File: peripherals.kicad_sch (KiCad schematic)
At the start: 15 parts, among them J10 Cam 3, J11 Servo, J12 Cam 2, J2 Encoder, J9 Cam 1, Q1 BSS816NWH6327XTSA1, Q2 NPN, Q3 BSS816NWH6327XTSA1, Q6 BSS816NWH6327XTSA1

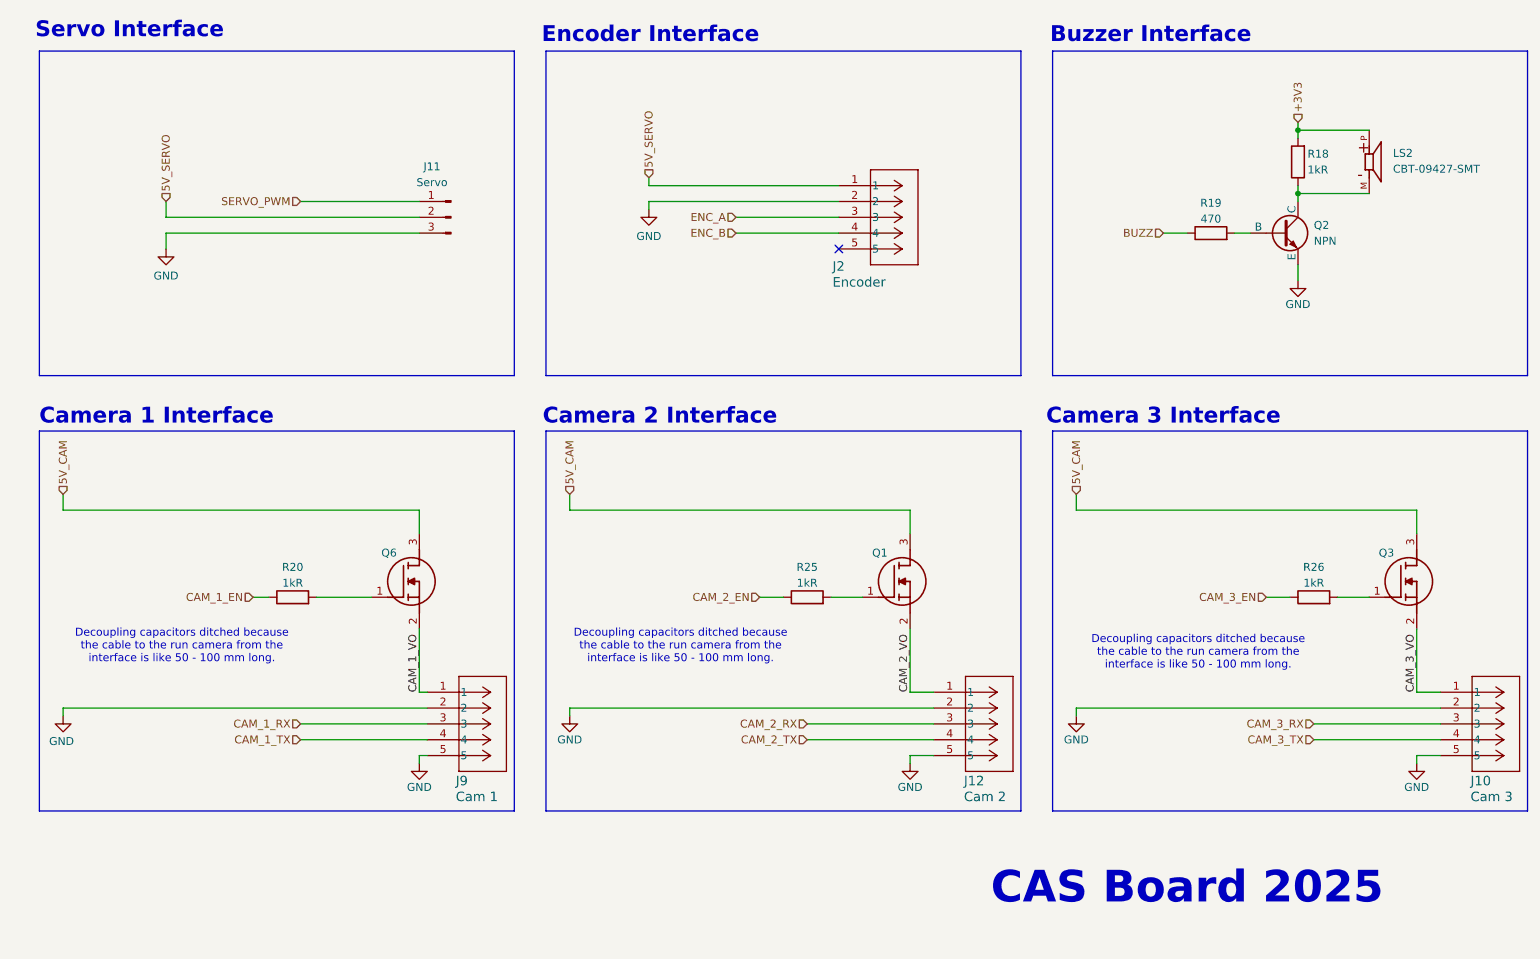
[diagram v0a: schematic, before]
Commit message: remove camera power and interface headers and pins from schematic and PCB
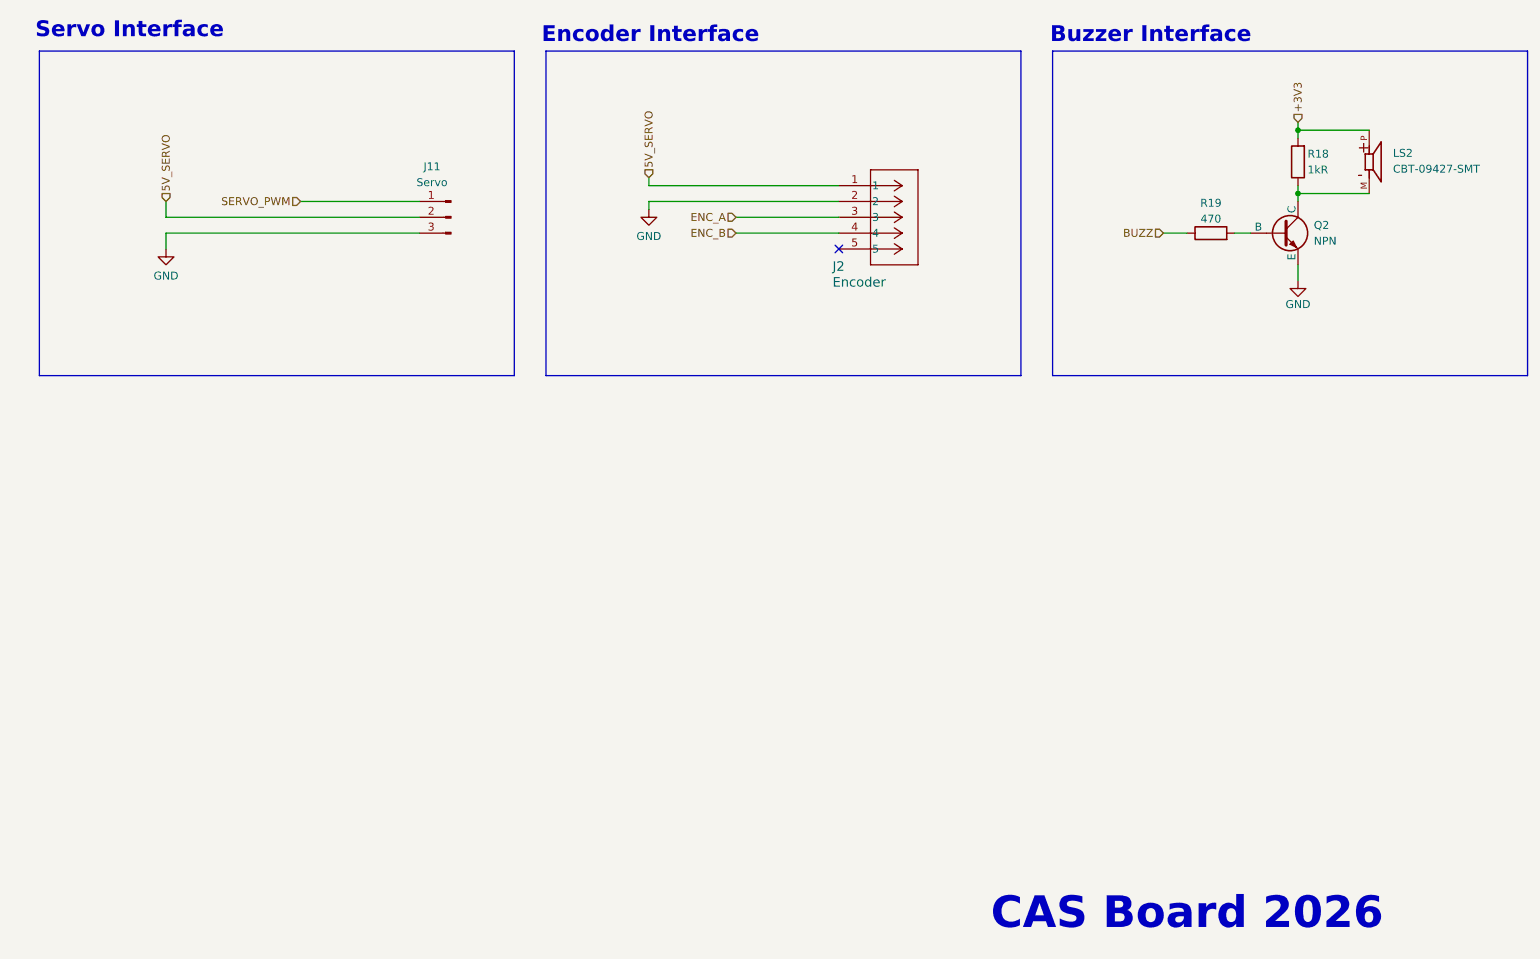
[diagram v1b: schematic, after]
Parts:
- removed J10: Cam 3, S05B_PASK_2_LF__SN_:CONN_S05B-PASK-2_JST, symbol 2025-06-21_05-21-07:S05B-PASK-2LFSN
- removed J12: Cam 2, S05B_PASK_2_LF__SN_:CONN_S05B-PASK-2_JST, symbol 2025-06-21_05-21-07:S05B-PASK-2LFSN
- removed J9: Cam 1, S05B_PASK_2_LF__SN_:CONN_S05B-PASK-2_JST, symbol 2025-06-21_05-21-07:S05B-PASK-2LFSN
- removed Q1, Q3: BSS816NWH6327XTSA1, SOT65P210X100-3N, symbol BSS816NWH6327XTSA1:BSS816NWH6327XTSA1
- removed Q6: BSS816NWH6327XTSA1, BSS816NWH6327XTSA1:SOT65P210X100-3N, symbol BSS816NWH6327XTSA1:BSS816NWH6327XTSA1
- removed R20, R25, R26: 1kR, Resistor_SMD:R_0805_2012Metric_Pad1.20x1.40mm_HandSolder, symbol Device:R
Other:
- note added: "CAS Board 2026"
- note removed: "CAS Board 2025"
- note removed: "Camera 1 Interface"
- note removed: "Camera 2 Interface"
- note removed: "Camera 3 Interface"
- note removed: "Decoupling capacitors ditched because the cable to the run camera from the interface is like 50 - 100 mm long."
